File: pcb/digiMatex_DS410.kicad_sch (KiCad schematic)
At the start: 21 parts, among them J1 POWER, J2 E, J3 A/B, Q1 PN2222A, U1 MAX7219

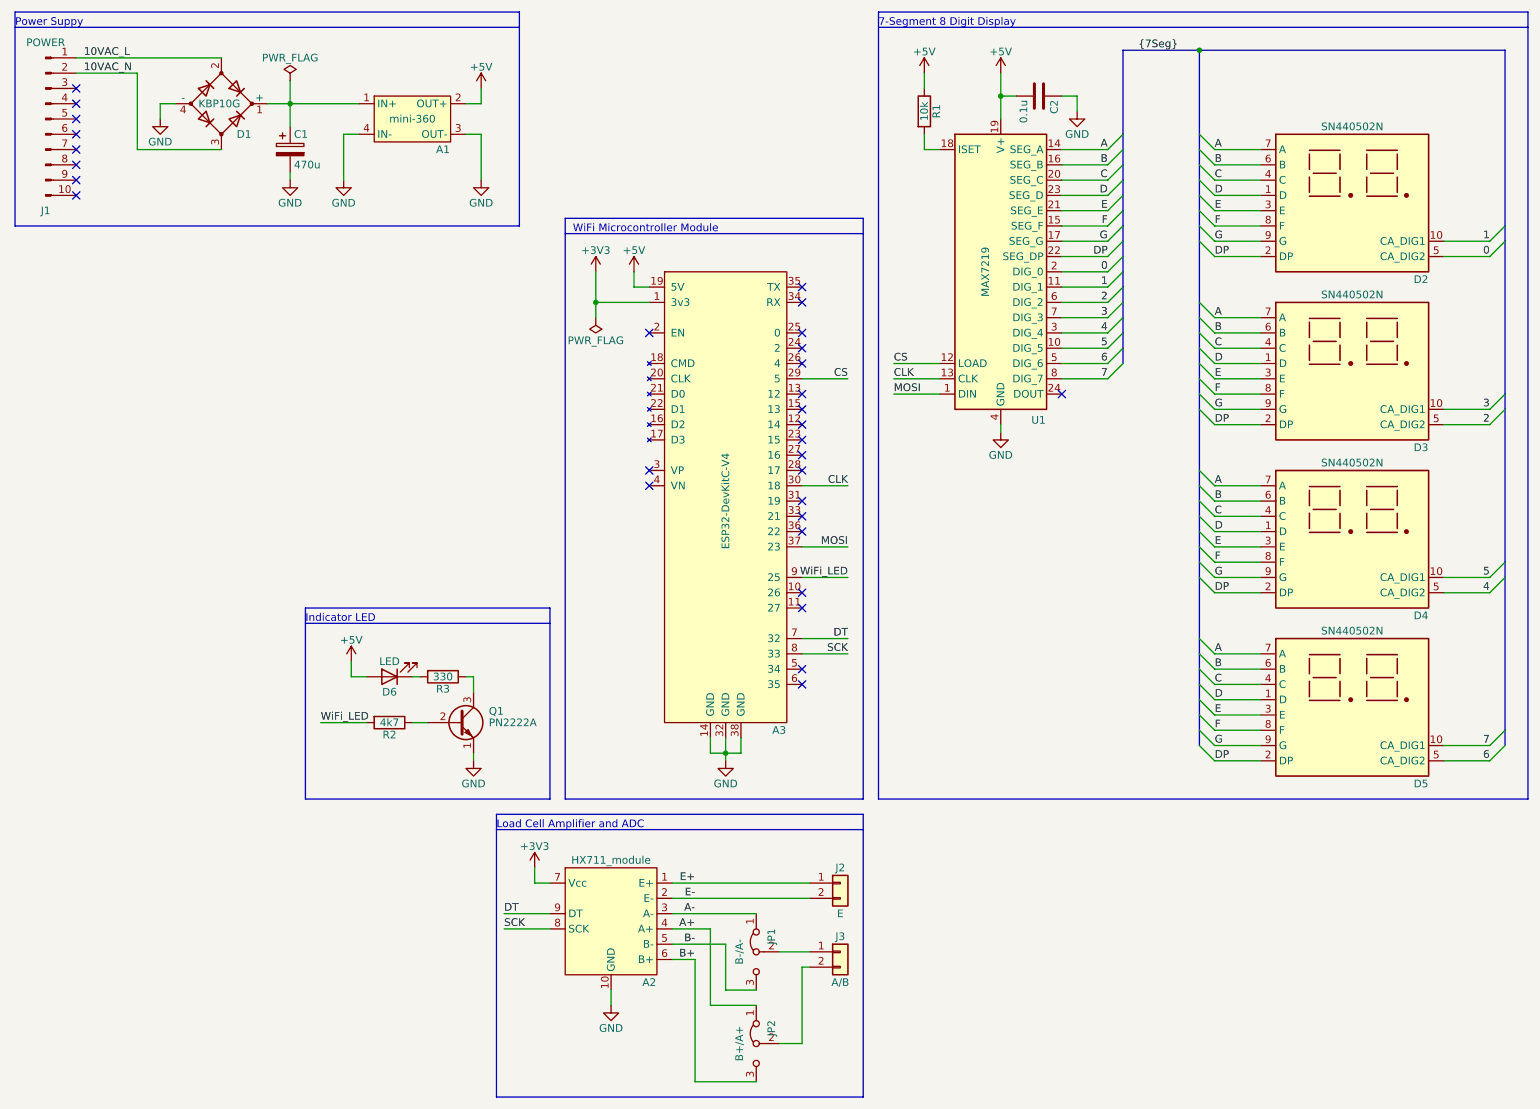
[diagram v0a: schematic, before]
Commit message: add mounts, buttons, and LEDs
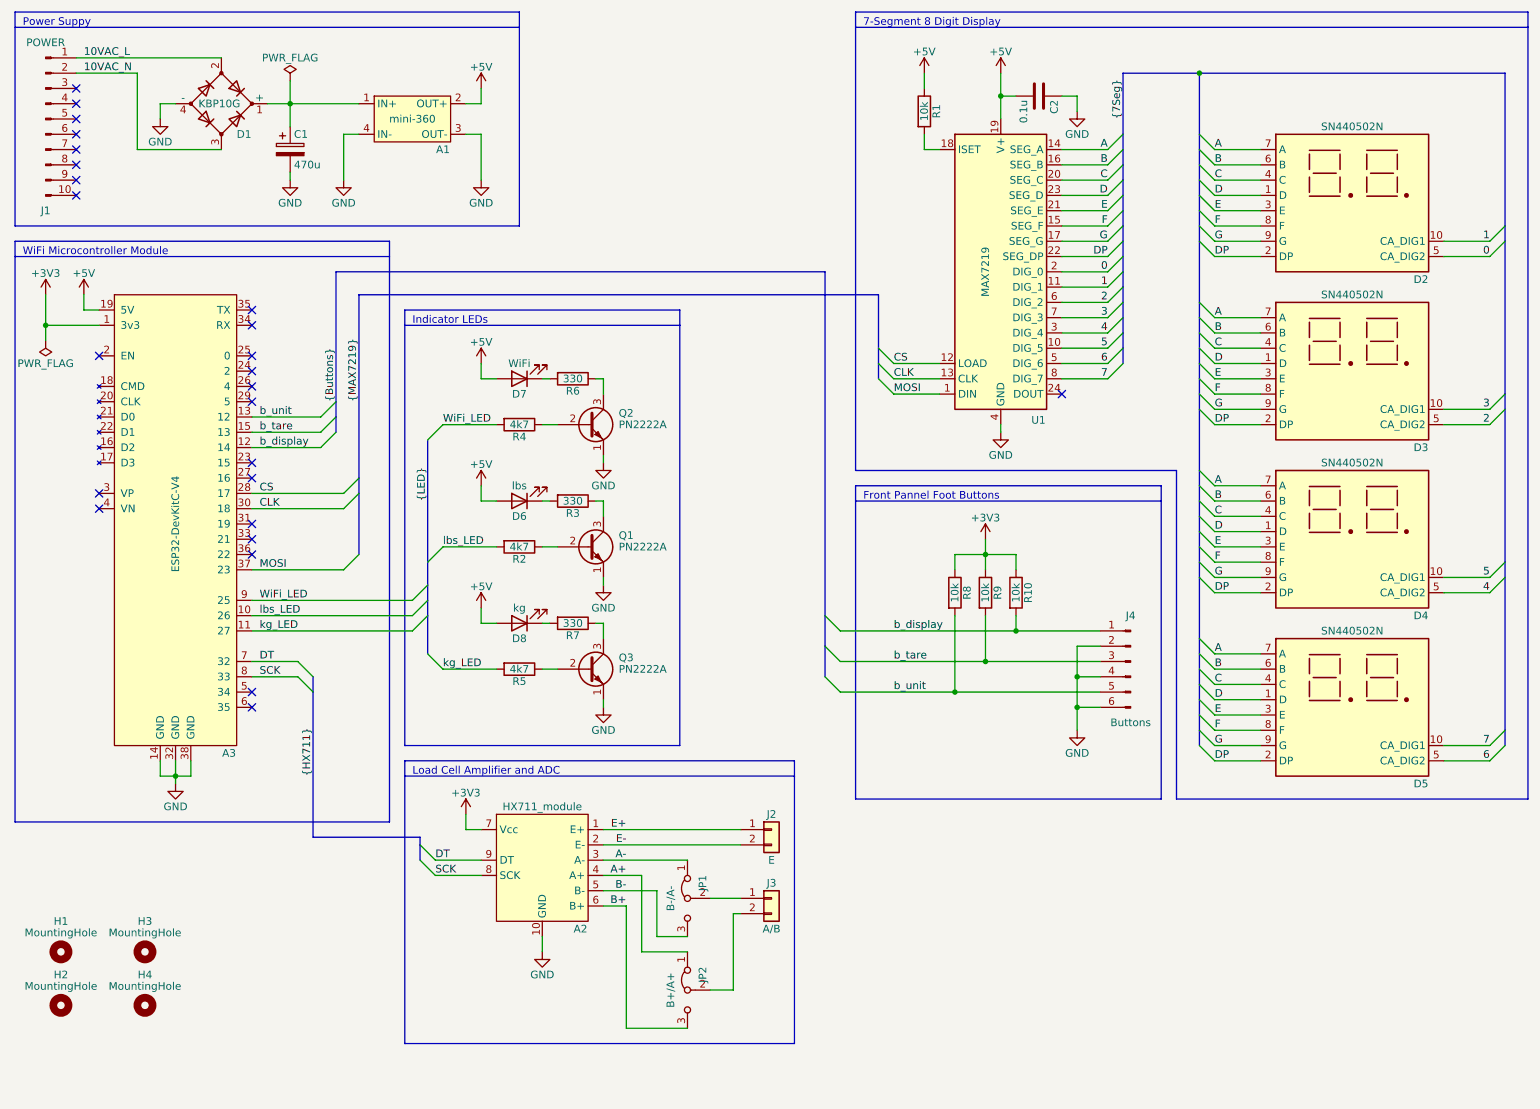
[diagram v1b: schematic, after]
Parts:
- added D7: WiFi, LED_THT:LED_D5.0mm, symbol Device:LED
- added D8: kg, LED_THT:LED_D5.0mm, symbol Device:LED
- added H1, H2, H3, H4: MountingHole, MountingHole:MountingHole_4mm_Pad, symbol Mechanical:MountingHole
- added J4: Buttons, Connector_Molex:Molex_KK-254_AE-6410-06A_1x06_P2.54mm_Vertical, symbol Connector:Conn_01x06_Male
- added Q2, Q3: PN2222A, Package_TO_SOT_THT:TO-92_Inline, symbol Transistor_BJT:PN2222A
- added R10, R8, R9: 10k, Resistor_THT:R_Axial_DIN0207_L6.3mm_D2.5mm_P15.24mm_Horizontal, symbol Device:R
- added R4, R5: 4k7, Resistor_THT:R_Axial_DIN0207_L6.3mm_D2.5mm_P15.24mm_Horizontal, symbol Device:R
- added R6, R7: 330, Resistor_THT:R_Axial_DIN0207_L6.3mm_D2.5mm_P15.24mm_Horizontal, symbol Device:R
- D6: value LED -> lbs
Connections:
- net +3V3: now also R10.1, R8.1, R9.1
- net +5V: now also D7.2 (A), D8.2 (A)
- net CS: now also A3.28 (17); no longer A3.29 (5)
- net GND: now also J4.2 (Pin_2), J4.4 (Pin_4), J4.6 (Pin_6), Q2.1 (E), Q3.1 (E)
- net WiFi_LED: now also R4.2; no longer R2.2
- net lbs_LED: now reaches A3.10 (26)
- net lbs_LED: now also R2.2
- net kg_LED: now reaches A3.11 (27)
- net kg_LED: now also R5.2
- net b_display: now reaches A3.12 (14)
- net b_display: now also J4.1 (Pin_1), R10.2
- net b_unit: now reaches A3.13 (12)
- net b_unit: now also J4.5 (Pin_5), R8.2
- net b_tare: now reaches A3.15 (13)
- net b_tare: now also J4.3 (Pin_3), R9.2
- new net: Q3.3 (C), R7.1
- new net: D8.1 (K), R7.2
- new net: Q3.2 (B), R5.1
- new net: D7.1 (K), R6.2
- new net: Q2.2 (B), R4.1
- new net: Q2.3 (C), R6.1
- no-connect marks 30 -> 25
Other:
- note added: "Front Pannel Foot Buttons"
- note added: "Indicator LEDs"
- note removed: "Indicator LED"
- moved on the sheet: A2, A3, D6, J2, J3, JP1, JP2, Q1, R2, R3

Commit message: replace mini-360 with 7805 regulator
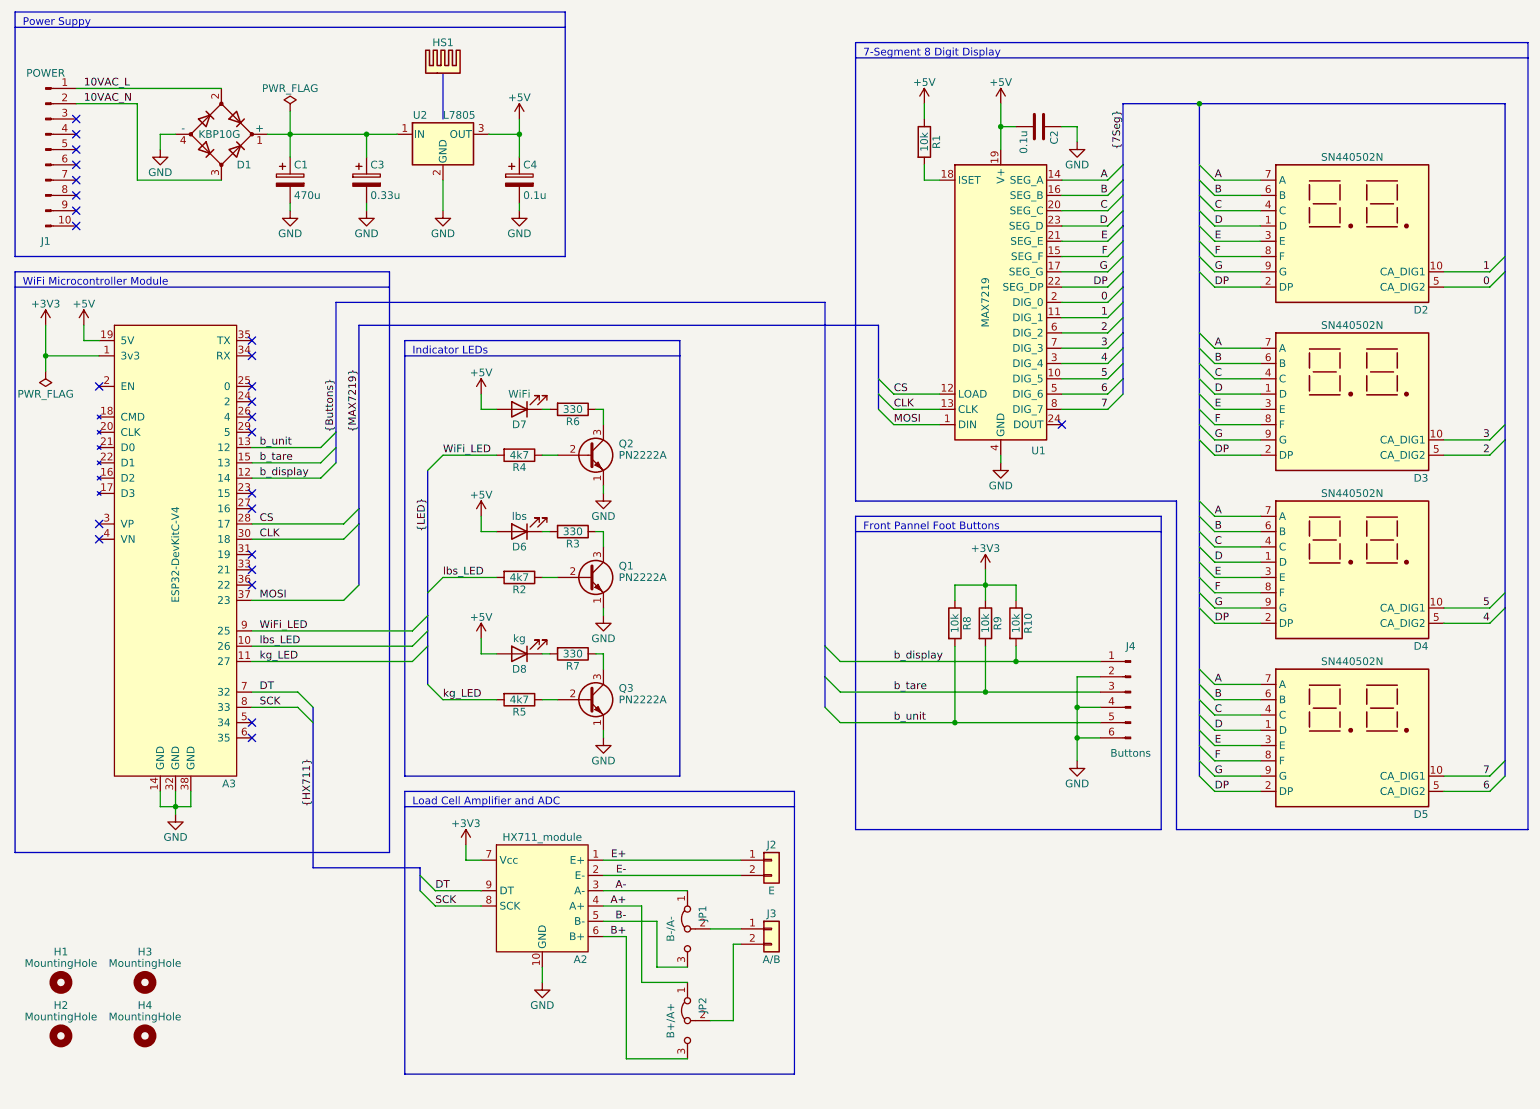
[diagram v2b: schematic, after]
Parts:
- removed A1: mini-360, pl_dcdc:mini-360, symbol pl_dcdc:mini-360
- added C3: 0.33u, Capacitor_THT:CP_Radial_D6.3mm_P2.50mm, symbol Device:C_Polarized
- added C4: 0.1u, Capacitor_THT:CP_Radial_D6.3mm_P2.50mm, symbol Device:C_Polarized
- added HS1: Heatsink, pl_heatsink:TO-220hs_16x16x25mm_2pins, symbol Mechanical:Heatsink
- added U2: L7805, Package_TO_SOT_THT:TO-220-3_Vertical, symbol Regulator_Linear:L7805
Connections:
- net +5V: now also C4.1, U2.3 (OUT)
- net GND: now also C3.2, C4.2, U2.2 (GND)
- net at C1.1, D1.1 (+): now also C3.1, U2.1 (IN)
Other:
- moved on the sheet: A2, A3, C1, C2, D1, D2, D3, D4, D5, D6, D7, D8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

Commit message: export pdf
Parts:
- removed R10, R8, R9: 10k, Resistor_THT:R_Axial_DIN0207_L6.3mm_D2.5mm_P15.24mm_Horizontal, symbol Device:R
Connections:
- net DT: now also A3.8 (33); no longer A3.7 (32)
- net SCK: now also A3.7 (32); no longer A3.8 (33)
- net b_display: now also A3.26 (4); no longer A3.12 (14)
- net b_tare: now also A3.23 (15), J4.5 (Pin_5); no longer A3.15 (13), J4.3 (Pin_3)
- net b_unit: now also A3.24 (2), J4.3 (Pin_3); no longer A3.13 (12), J4.5 (Pin_5)
